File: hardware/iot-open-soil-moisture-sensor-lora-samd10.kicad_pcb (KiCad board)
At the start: 2 copper layers, 43.5 x 67.5 mm, 40 parts, among them J1 ARM-JTAG-SWD-10, J2 Conn_01x04_Pin, J3 Conn_01x04_Pin, Q1 IRLML6401, Q2 NTJD1155LT1, U1 ATSAMD10D14A-SS, U2 TPD2E009DBZR, U3 TPD2E009DBZR, U4 Ai-Thinker-Ra-02, Y1 KX-327NHT

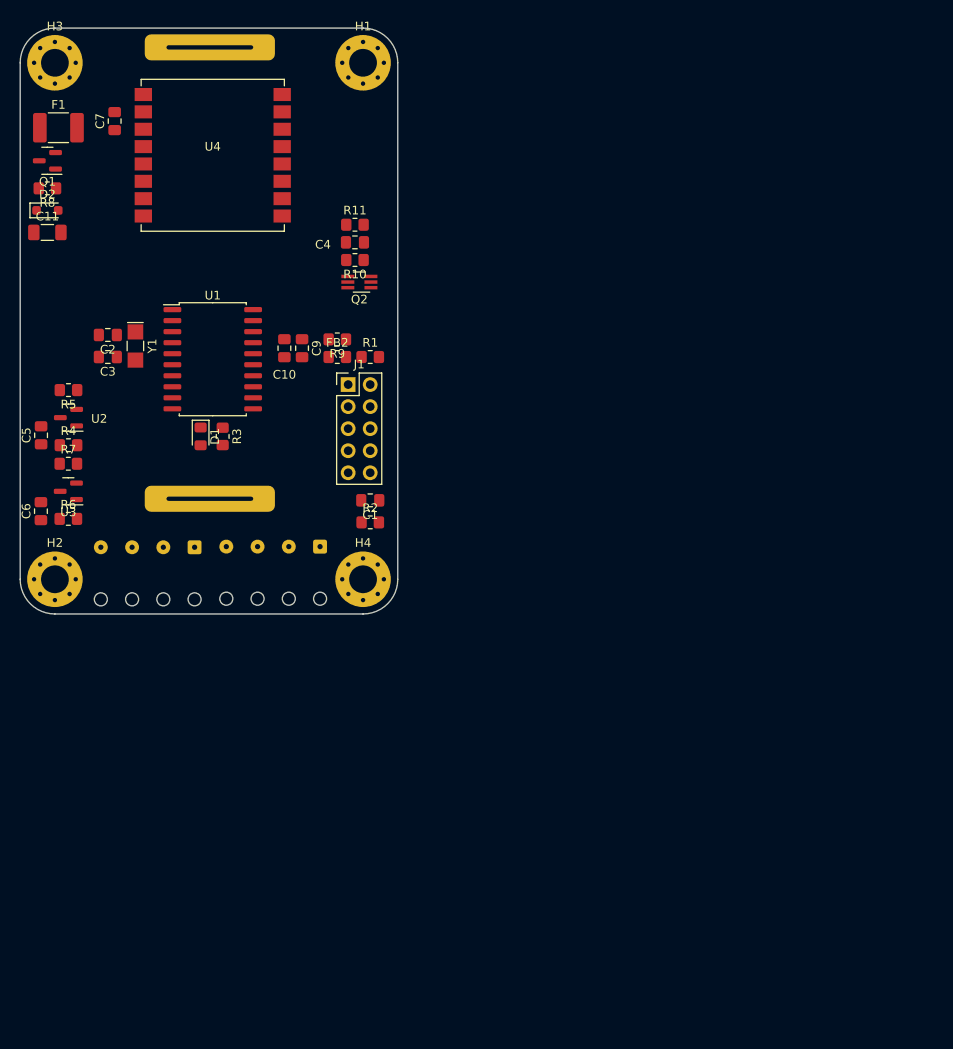
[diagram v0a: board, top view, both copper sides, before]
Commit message: add PCB signs
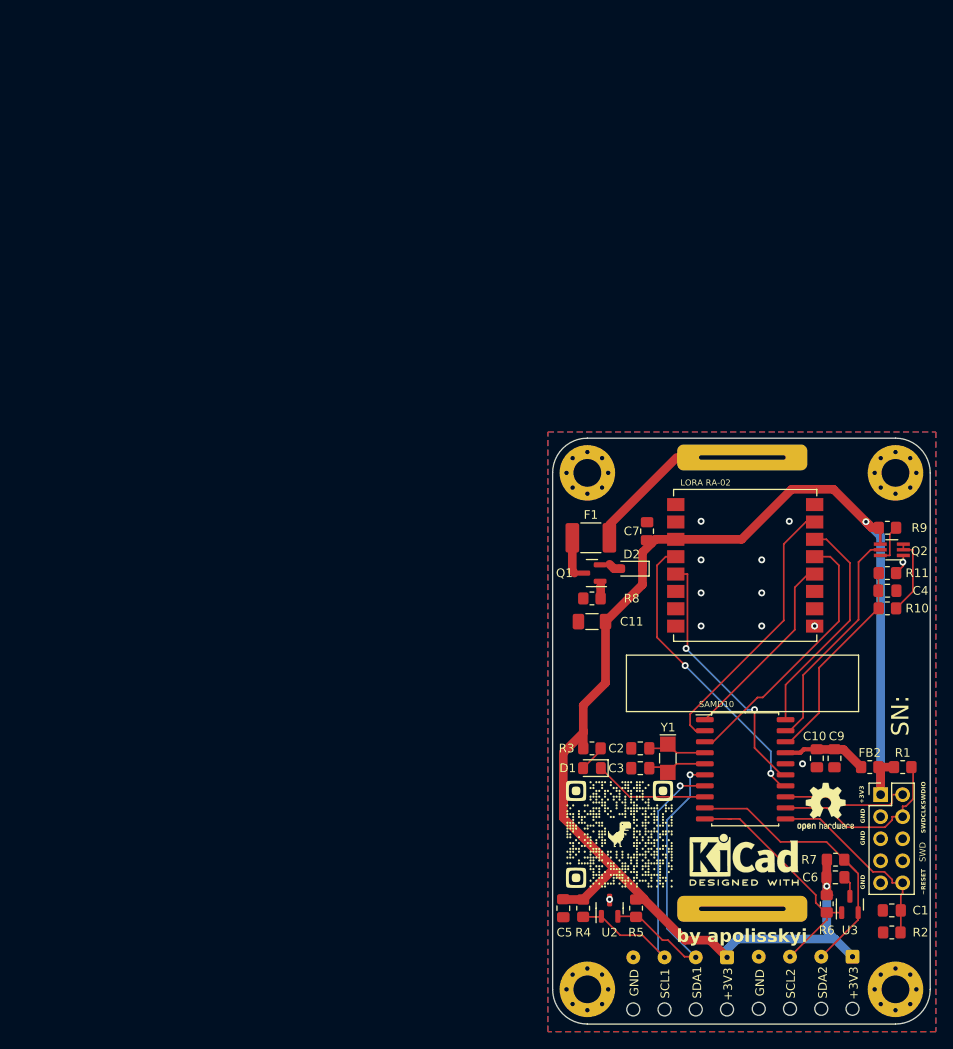
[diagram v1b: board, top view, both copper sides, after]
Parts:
- added G***: LOGO, LOGO, F.Cu at (130.0, 111.9)
- added REF**: OSHW-Logo2_7.3x6mm_SilkScreen, Symbol:OSHW-Logo2_7.3x6mm_SilkScreen, F.Cu at (153.8, 108.7)
- added REF**: KiCad-Logo2_5mm_SilkScreen, Symbol:KiCad-Logo2_5mm_SilkScreen, F.Cu at (144.4, 114.8)
- LORA RA-02: renamed from U4
- moved U3 101.8 mm to (156.6, 120.0), turned to 90 degrees
- moved C6 100.8 mm to (154.9, 116.8), turned to 0 degrees
- moved R7 99.5 mm to (154.9, 114.8)
- moved R6 98.0 mm to (153.9, 119.9), turned to -90 degrees
- moved R5 88.5 mm to (132.0, 120.4), turned to -90 degrees
- moved U2 84.1 mm to (128.9, 120.4), turned to 90 degrees
- moved C5 81.2 mm to (123.6, 120.4), turned to -90 degrees
- moved R4 79.8 mm to (125.9, 120.4), turned to -90 degrees
- moved D2 79.0 mm to (131.4, 81.3), turned to 180 degrees
- moved Q1 78.7 mm to (126.9, 81.8)
- moved R8 78.5 mm to (126.9, 84.7)
- moved C2 77.7 mm to (132.4, 102.0)
- moved Y1 77.6 mm to (135.6, 103.1)
- moved C3 77.5 mm to (132.4, 104.3)
- moved SAMD10 77.4 mm to (144.5, 104.4)
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- renumbered U1 to SAMD10, J1 to SWD
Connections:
- R2 pad 1: +3V3 -> +3V0
- R3 pad 1: +3V0 -> +3V3
- R4 pad 2: SDA1 -> SCL1
- R5 pad 2: SCL1 -> SDA1
- R6 pad 2: SDA2 -> SCL2
- R7 pad 2: SCL2 -> SDA2
- U2 pad 1: SDA1 -> SCL1
- U2 pad 2: SCL1 -> SDA1
- U3 pad 1: SDA2 -> SCL2
- U3 pad 2: SCL2 -> SDA2
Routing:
- net +3V3: track 0.00 -> 171.4 mm, vias 0 -> 2
- net SDA1: track 0.00 -> 37.3 mm, vias 0 -> 1
- net SCL1: track 0.00 -> 35.3 mm, vias 0 -> 1
- net ~{LORA_RESET}: track 0.00 -> 34.4 mm, vias 0 -> 2
- net SDA2: track 0.00 -> 34.0 mm
- net ~{LORA_CS}: track 0.00 -> 31.9 mm
- net MISO: track 0.00 -> 30.8 mm
- net LORA_IRQ: track 0.00 -> 30.1 mm, vias 0 -> 2
- net SCL2: track 0.00 -> 27.9 mm
- net MOSI: track 0.00 -> 26.3 mm
- net BAT_ADC_EN: track 0.00 -> 26.3 mm
- net BAT_ADC: track 0.00 -> 24.2 mm
- net ~RESET: track 0.00 -> 22.6 mm
- net SCK: track 0.00 -> 22.5 mm
- net SWDCLK: track 0.00 -> 21.7 mm
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- added copper zone on B.Cu, net GND
- added copper zone on F.Cu, net GND
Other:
- board text added: "+3V3"
- board text added: "GND"
- board text added: "SCL1"
- board text added: "SCL2"
- board text added: "SDA1"
- board text added: "SDA2"
- board text added: "SN:"
- board text added: "SWDCLK"
- board text added: "SWDIO"
- board text added: "by apolisskyi"
- board text added: "https://github.com/polesskiy-dev/iot-open-soil-moisture-sensor-lora-samd10"
- board text added: "~RESET"
